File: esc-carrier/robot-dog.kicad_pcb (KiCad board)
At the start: 2 copper layers, 74.3 x 78.1 mm, 38 parts, among them J1 Conn_01x02, J10 Conn_01x02, J11 Conn_01x04, J12 Conn_01x04, J13 Conn_01x04, J2 Conn_01x04, J3 Conn_01x04, J4 Conn_01x03, J5 Conn_01x05, J6 Conn_01x05, J7 Conn_01x05, J8 Conn_01x02, J9 Conn_01x02, SW1 SW_DIP_x02

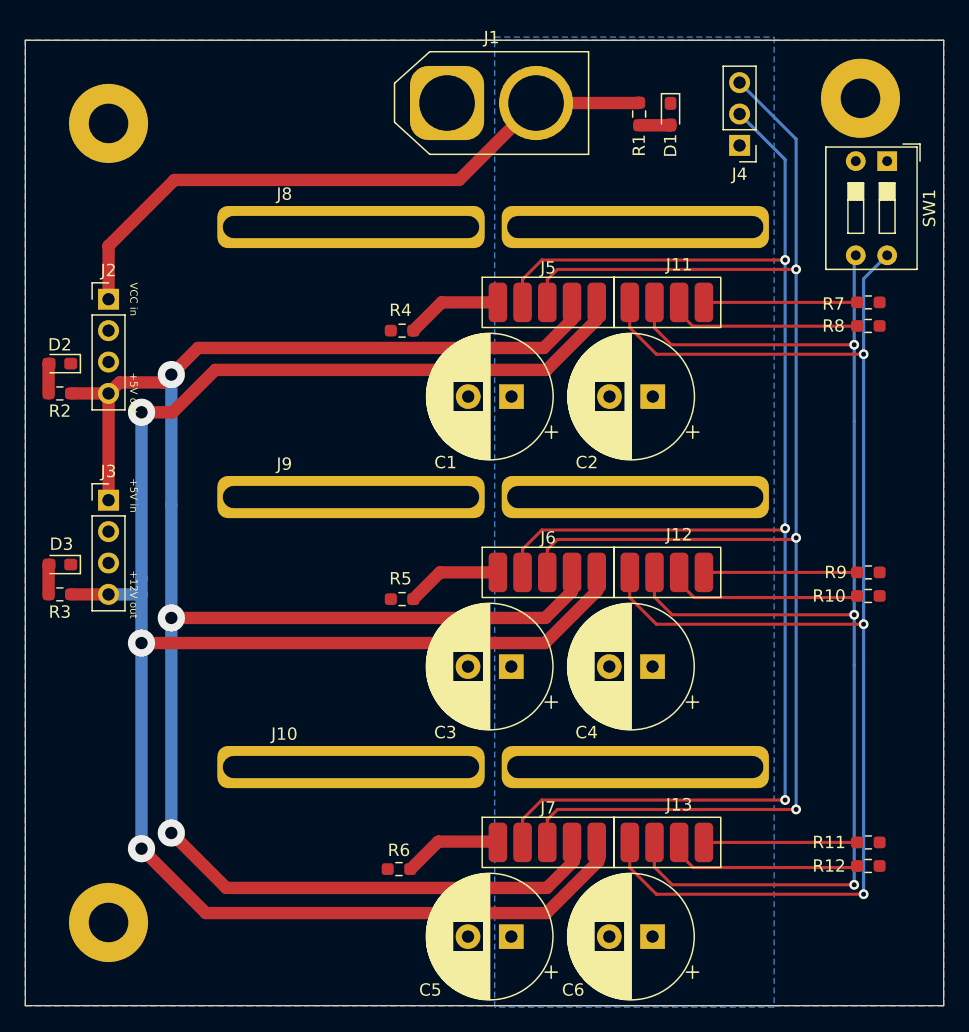
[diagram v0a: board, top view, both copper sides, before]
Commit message: update PCB layout for i2c pullup/pin change and debugging pins
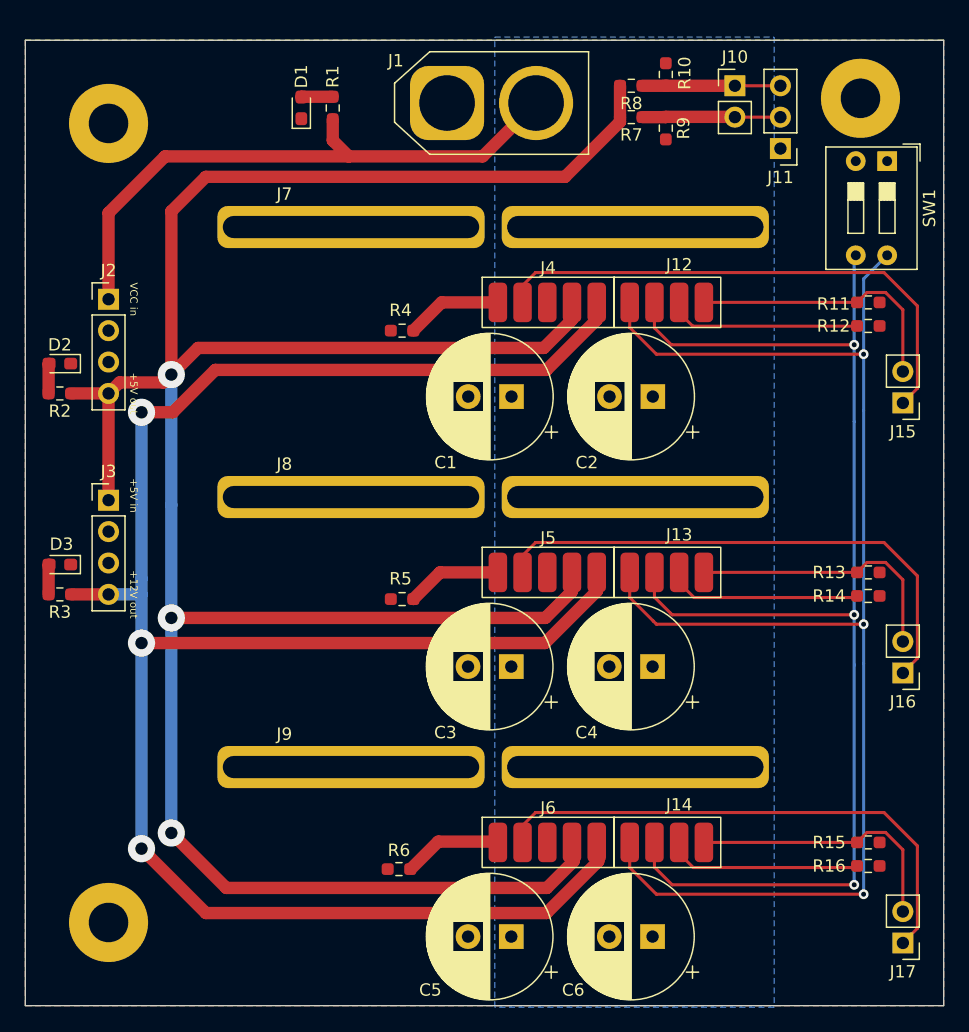
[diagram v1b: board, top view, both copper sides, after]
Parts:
- added J10: Conn_01x02, Connector_PinHeader_2.54mm:PinHeader_1x02_P2.54mm_Vertical, F.Cu at (187.3, 39.8)
- added J15: Conn_01x02, Connector_PinHeader_2.54mm:PinHeader_1x02_P2.54mm_Vertical, F.Cu at (200.9, 65.4)
- added J16: Conn_01x02, Connector_PinHeader_2.54mm:PinHeader_1x02_P2.54mm_Vertical, F.Cu at (200.9, 87.3)
- added J17: Conn_01x02, Connector_PinHeader_2.54mm:PinHeader_1x02_P2.54mm_Vertical, F.Cu at (200.9, 109.1)
- added R10: 10k, Resistor_SMD:R_0603_1608Metric_Pad0.98x0.95mm_HandSolder, F.Cu at (181.7, 38.8)
- added R7: 4.7k, Resistor_SMD:R_0603_1608Metric_Pad0.98x0.95mm_HandSolder, F.Cu at (178.9, 42.3)
- added R8: 4.7k, Resistor_SMD:R_0603_1608Metric_Pad0.98x0.95mm_HandSolder, F.Cu at (178.9, 39.8)
- added R9: 10k, Resistor_SMD:R_0603_1608Metric_Pad0.98x0.95mm_HandSolder, F.Cu at (181.7, 43.2)
- moved D1 29.9 mm to (152.2, 41.5), turned to 90 degrees
- moved R1 24.8 mm to (154.8, 41.6), turned to 90 degrees
- moved J11 3.31 mm to (191.0, 44.8)
- renumbered J4 to J11, J11 to J12, J12 to J13, J13 to J14, J5 to J4, J6 to J5, J7 to J6, J8 to J7, J9 to J8, J10 to J9, R7 to R11, R8 to R12, R9 to R13, R10 to R14, R11 to R15, R12 to R16
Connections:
- net Net-(J11-Pad4) renamed PGD-0
- net Net-(J12-Pad4) renamed PGD-1
- net Net-(J13-Pad4) renamed PGD-2
- J11 pad 2: SCL -> scl-pullup
- J11 pad 3: SDA -> sda-pullup
- J4 pad 2: SCL -> PGC-0
- J4 pad 3: SDA -> unconnected-(J4-Pad3)
- J5 pad 2: SCL -> PGC-1
- J5 pad 3: SDA -> unconnected-(J5-Pad3)
- J6 pad 2: SCL -> PGC-2
- J6 pad 3: SDA -> unconnected-(J6-Pad3)
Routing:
- net SCL: track 128.3 -> 0.00 mm, vias 3 -> 0
- net SDA: track 127.6 -> 0.00 mm, vias 3 -> 0
- net +5V: track 161.5 -> 216.9 mm
- net PGC-2: track 0.00 -> 43.2 mm
- net PGC-0: track 0.00 -> 43.2 mm
- net PGC-1: track 0.00 -> 43.2 mm
- net scl-pullup: track 0.00 -> 11.2 mm
- net sda-pullup: track 0.00 -> 11.2 mm
- net PGD-0: track 12.4 -> 22.0 mm
- net PGD-2: track 12.4 -> 22.0 mm
- net PGD-1: track 12.4 -> 22.0 mm
- net VCC: track 52.0 -> 48.8 mm
